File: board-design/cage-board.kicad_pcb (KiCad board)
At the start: 2 copper layers, 160 x 160 mm, 58 parts, among them J1 Jack-DC, J10 73131-0240, J11 73131-0240, J12 73131-0240, J13 Conn_01x02, J14 Conn_01x02, J15 Conn_02x13_test_points, J16 TB002-500-03BE, J17 TB002-500-03BE, J18 TB002-500-03BE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

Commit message: all done except moving J13
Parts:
- removed C3: 1uF, Capacitor_SMD:C_0805_2012Metric_Pad1.15x1.40mm_HandSolder
- removed C4: 10u 50V, Capacitor_SMD:C_1210_3225Metric_Pad1.33x2.70mm_HandSolder
- removed C5: 22u 10V, Capacitor_SMD:C_0805_2012Metric_Pad1.18x1.45mm_HandSolder
- removed LED1, LED2, LED3, LED4, LED5, LED6: LED, LED_THT:LED_Rectangular_W5.0mm_H2.0mm
- removed R11, R13, R14, R16, R9: 1k, Resistor_SMD:R_0805_2012Metric_Pad1.20x1.40mm_HandSolder
- removed R15: 10k, Resistor_SMD:R_0805_2012Metric_Pad1.20x1.40mm_HandSolder
- removed REF**: usb-6501-oem, chen-lab:usb-6501-oem
- removed U2: VX7805-500, Package_SIP:SIP3_11.6x8.5mm
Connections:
- J2 pad 33: Net-(J2-Pad33) -> +5V
- J2 pad 34: Net-(J2-Pad34) -> +5V
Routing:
- net /P1.0: track 86.6 -> 34.4 mm, vias 1 -> 0
- net +5V: track 36.6 -> 6.64 mm, vias 4 -> 1
- net /P1.3: track 160.1 -> 141.2 mm
- net /P1.2: track 174.4 -> 155.6 mm
- net Net-(LED3-Pad2): track 10.7 -> 0.00 mm, vias 1 -> 0
- net Net-(LED4-Pad2): track 6.67 -> 0.00 mm
- net +24V: track 12.2 -> 5.84 mm
- net GND: track 31.1 -> 25.2 mm, vias 7 -> 4
- net Net-(LED1-Pad2): track 5.34 -> 0.00 mm
- net Net-(LED2-Pad2): track 5.31 -> 0.00 mm
- net Net-(LED6-Pad2): track 5.01 -> 0.00 mm
- net Net-(LED5-Pad2): track 4.30 -> 0.00 mm

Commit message: Final Rev C layout
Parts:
- moved J13 3.56 mm to (198.1, 108.1)
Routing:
- net GND: track 25.2 -> 15.0 mm
- net Net-(D1-Pad1): track 37.9 -> 41.4 mm
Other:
- board text added: "Chen-Lab RevC (06/2021) edf.bu.edu"
- board text removed: "Chen-Lab RevB (01/2021) kremerme@bu.edu, edf.bu.edu"

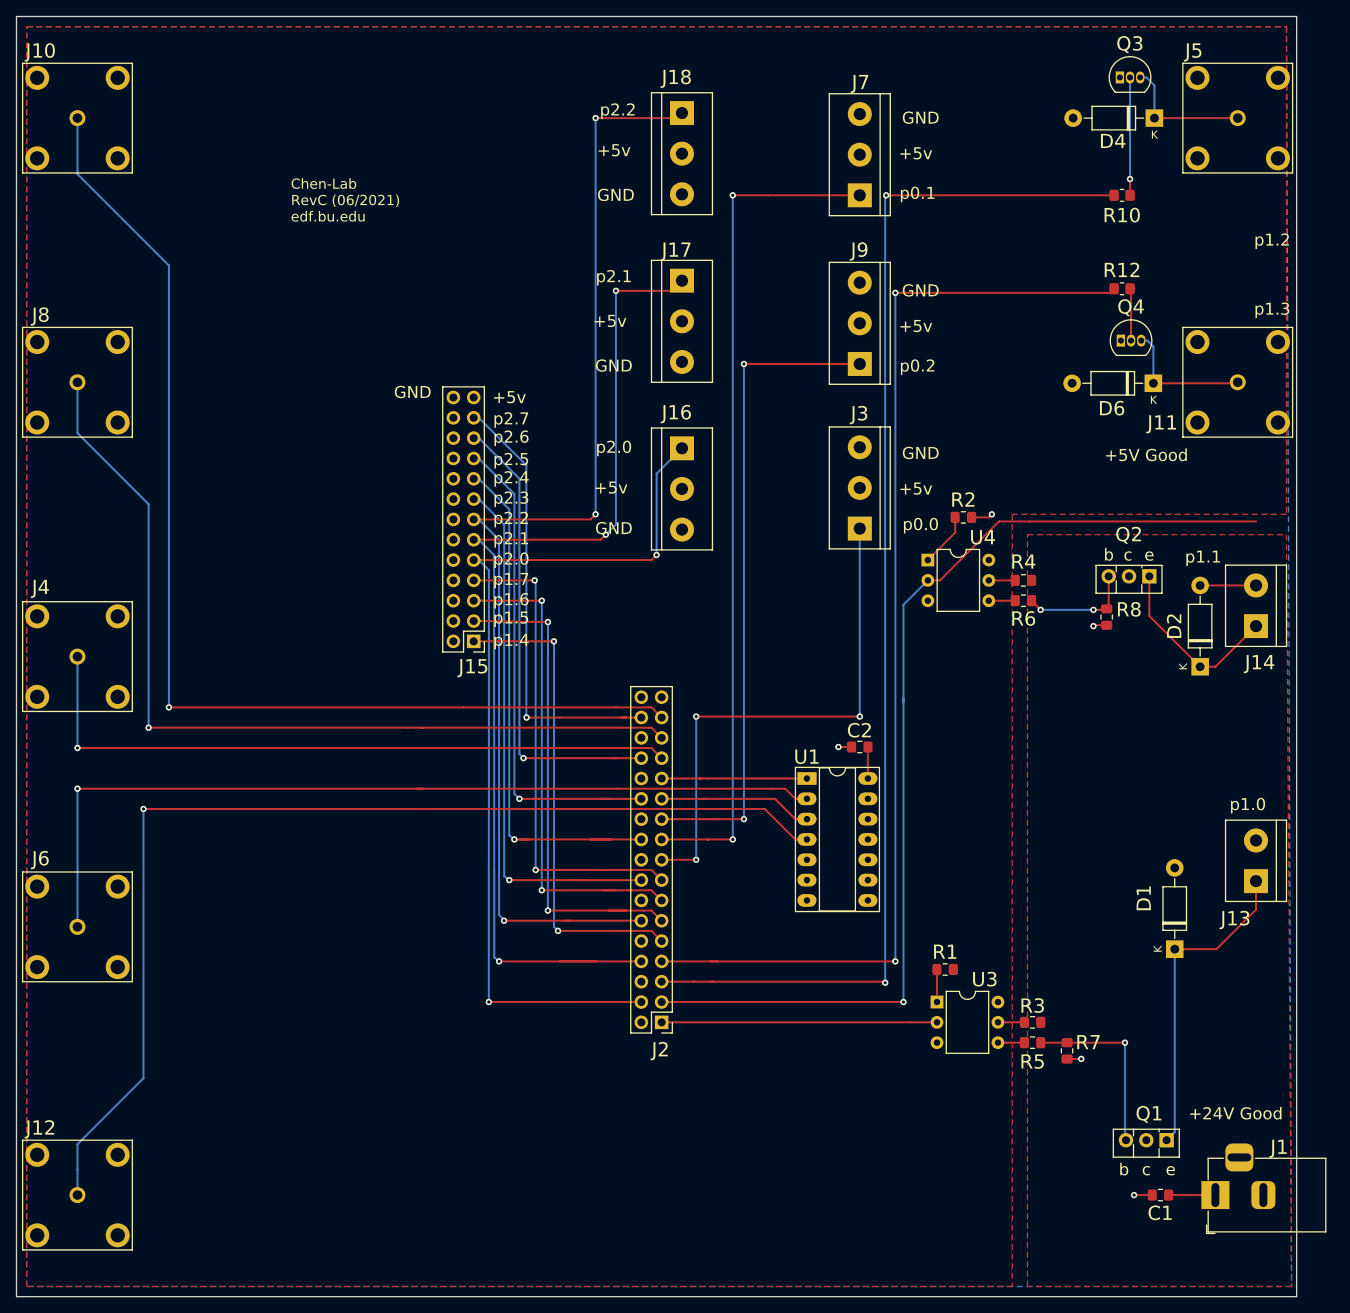
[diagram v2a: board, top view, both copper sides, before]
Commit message: Restore USB board footprint, tweak silkscreen
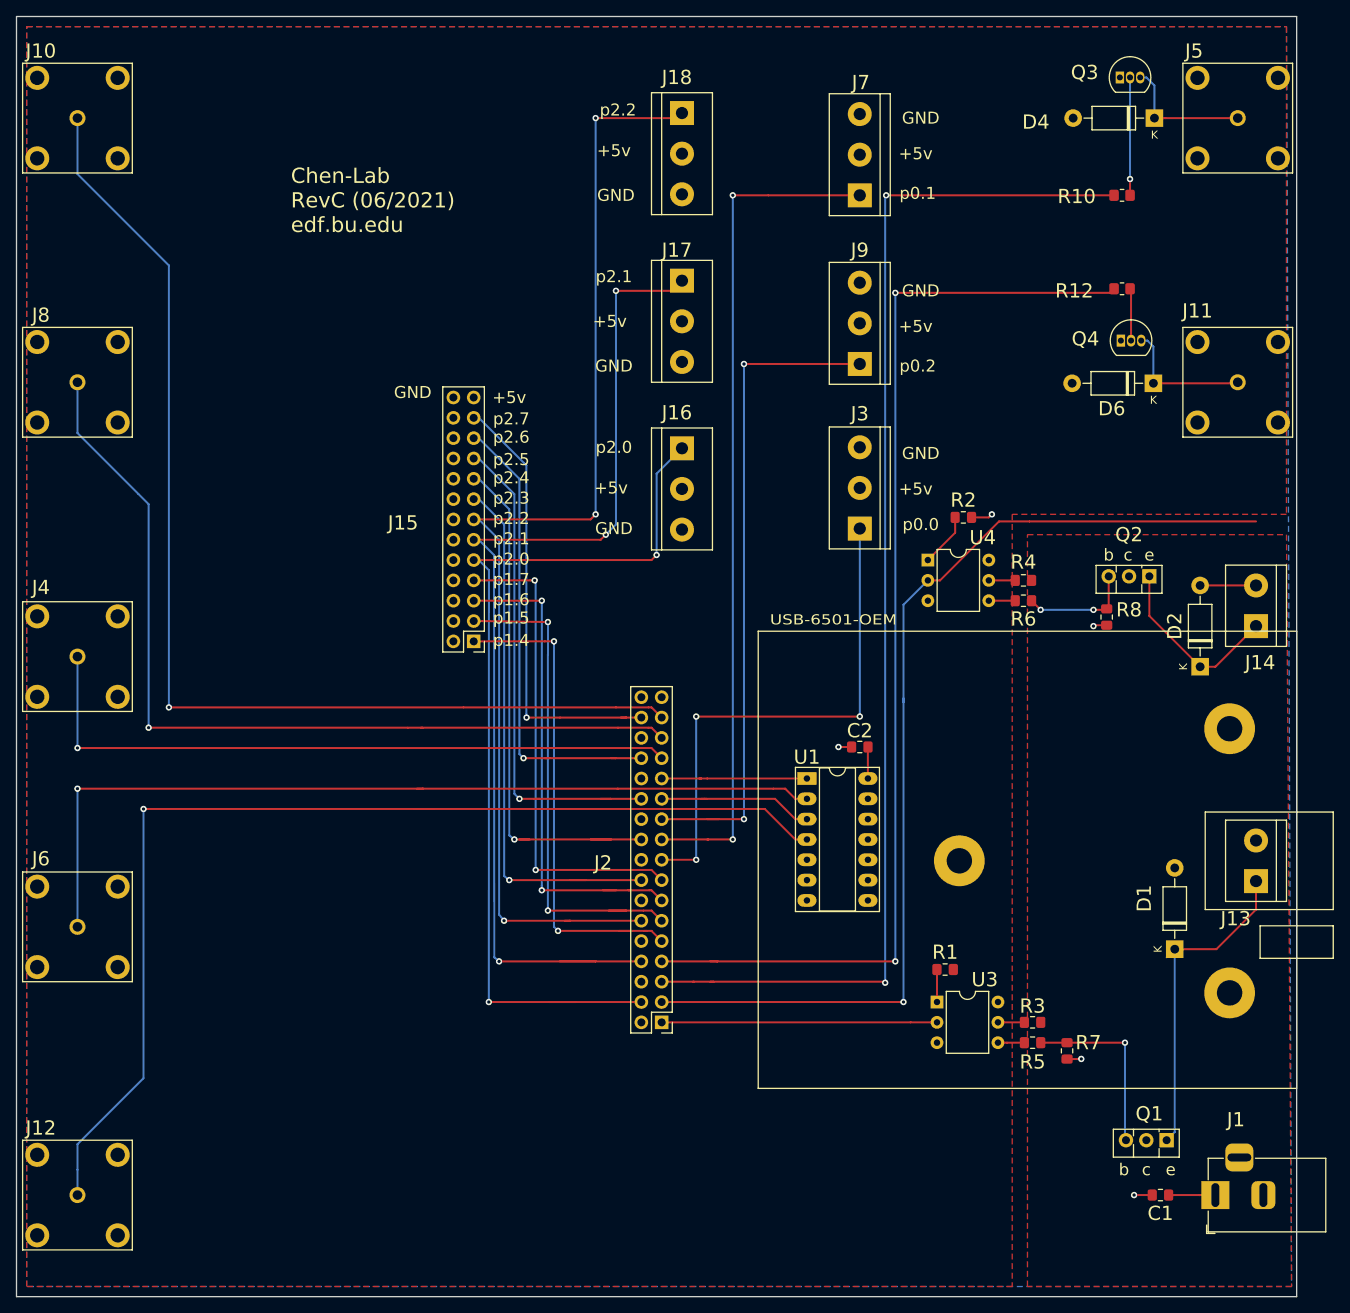
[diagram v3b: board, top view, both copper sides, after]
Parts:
- added USB-6501-OEM: usb-6501-oem, chen-lab:usb-6501-oem, F.Cu at (203.2, 76.8)
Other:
- board text removed: "+24V Good"
- board text removed: "+5V Good"
- board text removed: "p1.0"
- board text removed: "p1.1"
- board text removed: "p1.2"
- board text removed: "p1.3"
